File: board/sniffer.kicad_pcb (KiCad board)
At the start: 8 copper layers, 154 x 125 mm, 321 parts, among them J1 BARREL, J10 CONN_SFP_HOST, J11 SFP_CAGE, J12 PMOD_HOST, J13 CONN_SATA_DEVICE, J14 CONN_SATA_HOST, J15 CONN_LVDS_EXPANSION_HOST, J2 32K243-40ML5, J3 BEL_FUSE_0826-1G1T-23-F, J4 XILINX_JTAG, J5 32K243-40ML5, J6 32K243-40ML5, J7 32K243-40ML5, J8 CONN_SFF8087, J9 CONN_SFF8087, M1 SCREW_HOLE, M2 SCREW_HOLE, M3 SCREW_HOLE, M4 SCREW_HOLE, Q1 SSM6N58NU, U1 OKL-T_3-W12P-C, U10 KSZ9031RN, U11 74AVCH1T45, U12 74AVCH1T45, U13 74AVCH1T45, U14 74AVCH1T45, U15 W25Q128JV, U16 FPF2498, U17 FPF2498, U18 LP2996A, U19 SIT9121AI-2BF-XXS200.000000G, U2 LTC3374-QFN, U3 MYTNA1R84RELA2RA, U4 DDR3_SODIMM, U5 XC7K70T-2FBG484, U6 ECX2-LMV-7CN-156.250-TR, U7 SIT9121AI-2BF-XXS200.000000G, U8 ECX2-LMV-3CN-125.000-TR, U9 ECS-2016MVQ-250-CN

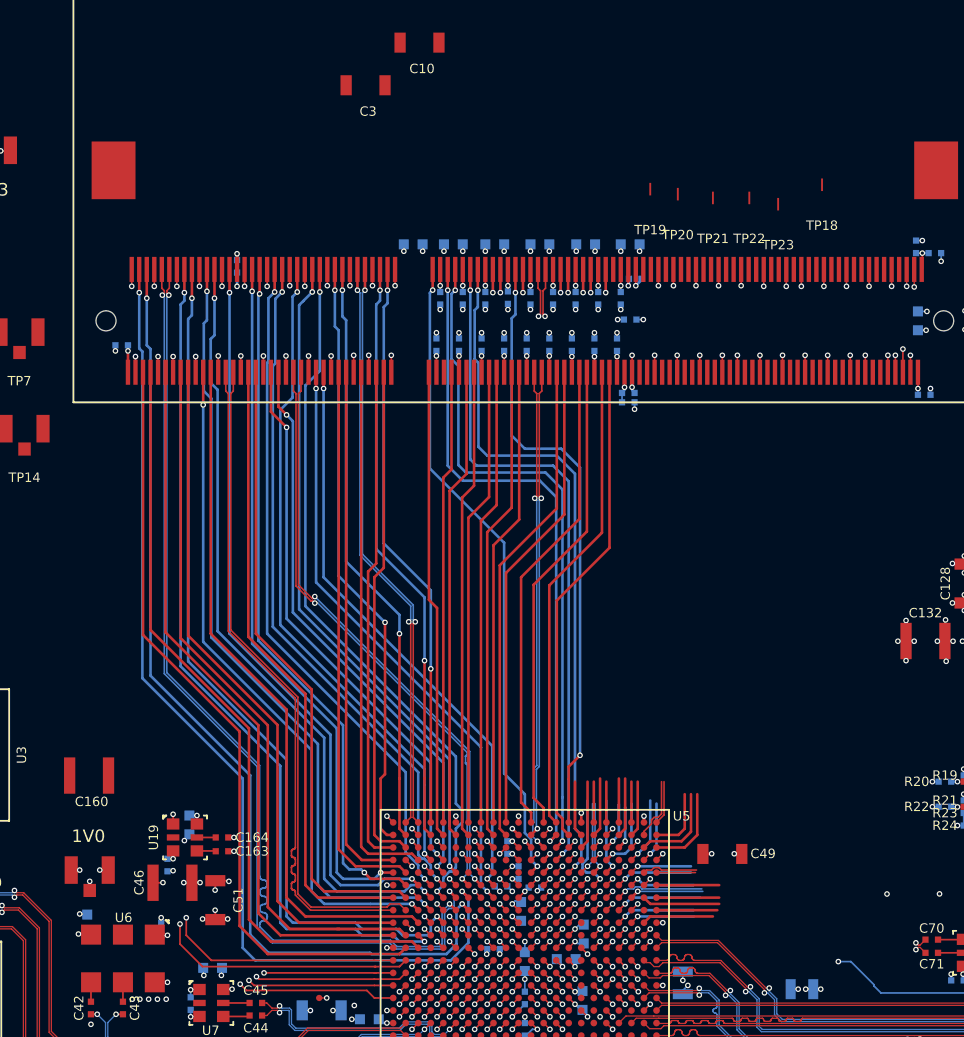
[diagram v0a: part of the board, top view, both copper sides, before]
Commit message: Fully routed DDR. Length matched first three DQ groups.
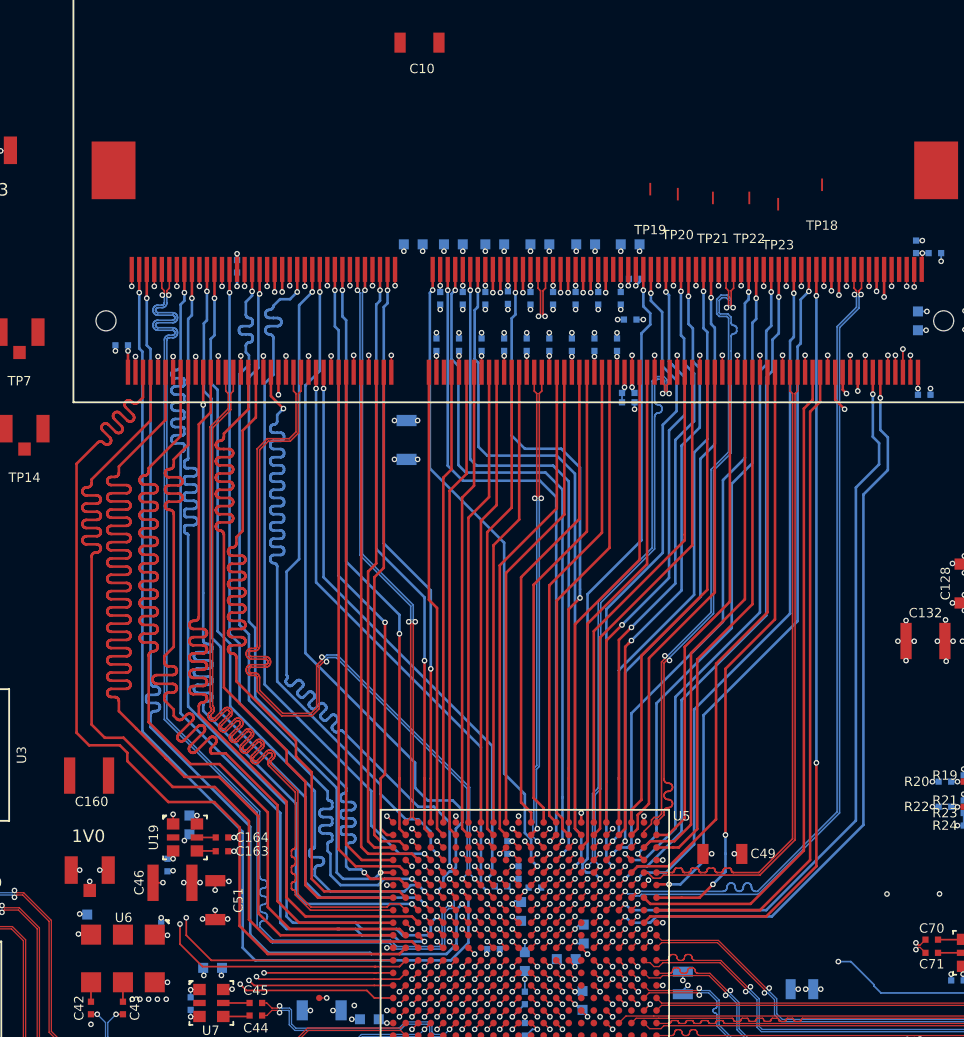
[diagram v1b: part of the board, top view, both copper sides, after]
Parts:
- C3: moved to B.Cu
- moved C3 28.5 mm to (99.5, 75.5), turned to 270 degrees
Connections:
- U5 pad AA16: /DDR/RAM_DQ6_5 -> /DDR/RAM_DQ6_2
- U5 pad AA19: /DDR/RAM_DQ5_3 -> /DDR/RAM_DQ5_7
- U5 pad AA20: /DDR/RAM_DQ5_1 -> /DDR/RAM_DQ5_2
- U5 pad AB16: /DDR/RAM_DQ6_4 -> /DDR/RAM_DQ6_1
- U5 pad AB20: /DDR/RAM_DQ5_4 -> /DDR/RAM_DQ5_3
- U5 pad AB21: /DDR/RAM_DQ5_2 -> /DDR/RAM_DM5
- U5 pad R16: /DDR/RAM_DQ7_0 -> /DDR/RAM_DQ7_4
- U5 pad T15: /DDR/RAM_DQ7_6 -> /DDR/RAM_DQ7_1
- U5 pad T16: /DDR/RAM_DQ7_1 -> /DDR/RAM_DQ7_5
- U5 pad T20: /DDR/RAM_DQ4_7 -> /DDR/RAM_DQ4_1
- U5 pad T21: /DDR/RAM_DM4 -> /DDR/RAM_DQ4_0
- U5 pad U16: /DDR/RAM_DM7 -> /DDR/RAM_DQ7_6
- U5 pad U17: /DDR/RAM_DQ4_5 -> /DDR/RAM_DQ4_4
- U5 pad U21: /DDR/RAM_DQ4_0 -> /DDR/RAM_DQ4_3
- U5 pad U22: /DDR/RAM_DQ4_1 -> /DDR/RAM_DQ4_2
- U5 pad V15: /DDR/RAM_DQ7_4 -> /DDR/RAM_DQ7_0
- U5 pad V18: /DDR/RAM_DQ4_6 -> /DDR/RAM_DQ4_5
- U5 pad V19: /DDR/RAM_DQ5_7 -> /DDR/RAM_DQ5_6
- U5 pad V20: /DDR/RAM_DQ5_5 -> /DDR/RAM_DQ5_4
- U5 pad V22: /DDR/RAM_DQ4_2 -> /DDR/RAM_DM4
- U5 pad W14: /DDR/RAM_DQ7_2 -> /DDR/RAM_DQ7_3
- U5 pad W15: /DDR/RAM_DQ7_5 -> /DDR/RAM_DQ7_2
- U5 pad W17: /DDR/RAM_DQ6_1 -> /DDR/RAM_DQ6_5
- U5 pad W20: /DDR/RAM_DQ5_6 -> /DDR/RAM_DQ5_5
- U5 pad W21: /DDR/RAM_DQ4_3 -> /DDR/RAM_DQ4_7
- U5 pad W22: /DDR/RAM_DQ4_4 -> /DDR/RAM_DQ4_6
- U5 pad Y14: /DDR/RAM_DQ7_3 -> /DDR/RAM_DM7
- U5 pad Y17: /DDR/RAM_DQ6_2 -> /DDR/RAM_DM6
- U5 pad Y18: /DDR/RAM_DM6 -> /DDR/RAM_DQ6_0
- U5 pad Y19: /DDR/RAM_DQ6_0 -> /DDR/RAM_DQ6_4
- U5 pad Y21: /DDR/RAM_DM5 -> /DDR/RAM_DQ5_1
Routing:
- net /Power Supply/1V0_GOOD: track 23.0 -> 118.0 mm
- net /DDR/RAM_DQS7_N: track 5.90 -> 64.9 mm, vias 1 -> 2
- net /DDR/RAM_DQS7_P: track 7.03 -> 64.9 mm, vias 1 -> 2
- net /DDR/RAM_DQ6_7: track 5.71 -> 63.2 mm, vias 0 -> 2
- net /DDR/RAM_DQ7_3: track 5.21 -> 60.3 mm, vias 1 -> 2
- net /DDR/RAM_DQ7_7: track 6.27 -> 61.0 mm, vias 1 -> 2
- net /DDR/RAM_DQ7_4: track 4.41 -> 58.8 mm, vias 1 -> 2
- net /DDR/RAM_DQ7_6: track 6.62 -> 59.4 mm, vias 1 -> 2
- net /DDR/RAM_DQ7_2: track 6.41 -> 59.0 mm, vias 1 -> 2
- net /DDR/RAM_DQ7_5: track 6.91 -> 58.6 mm, vias 1 -> 2
- net /DDR/RAM_DM6: track 4.96 -> 55.5 mm, vias 1 -> 2
- net /DDR/RAM_DQ6_6: track 5.00 -> 55.2 mm, vias 0 -> 2
- net /DDR/RAM_DQ4_4: track 3.50 -> 52.7 mm, vias 0 -> 2
- net /DDR/RAM_DQ5_6: track 3.46 -> 52.2 mm, vias 1 -> 2
- net /DDR/RAM_DQ6_4: track 5.00 -> 53.7 mm, vias 0 -> 2
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
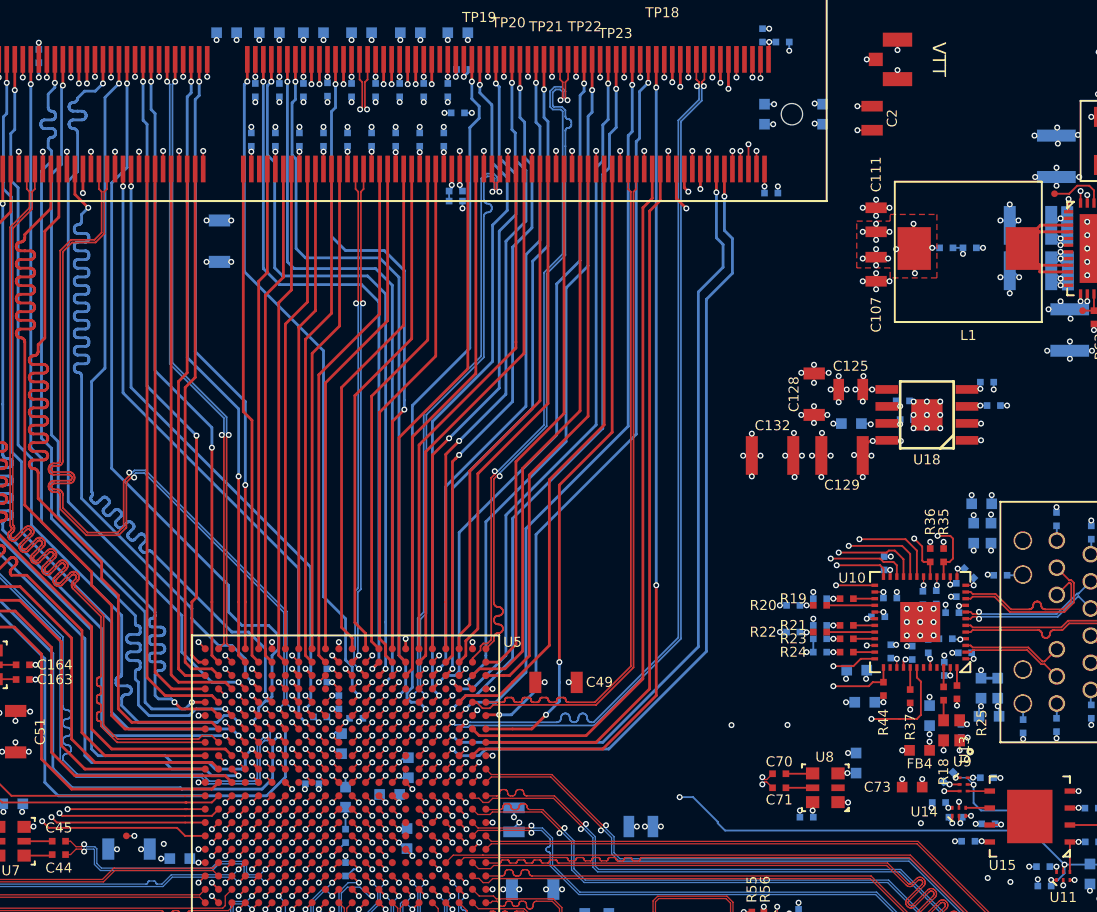
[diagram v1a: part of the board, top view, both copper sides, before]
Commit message: Continued work on layout. Finished length matchnig all DQ byte groups. Still have to do C/A bus.
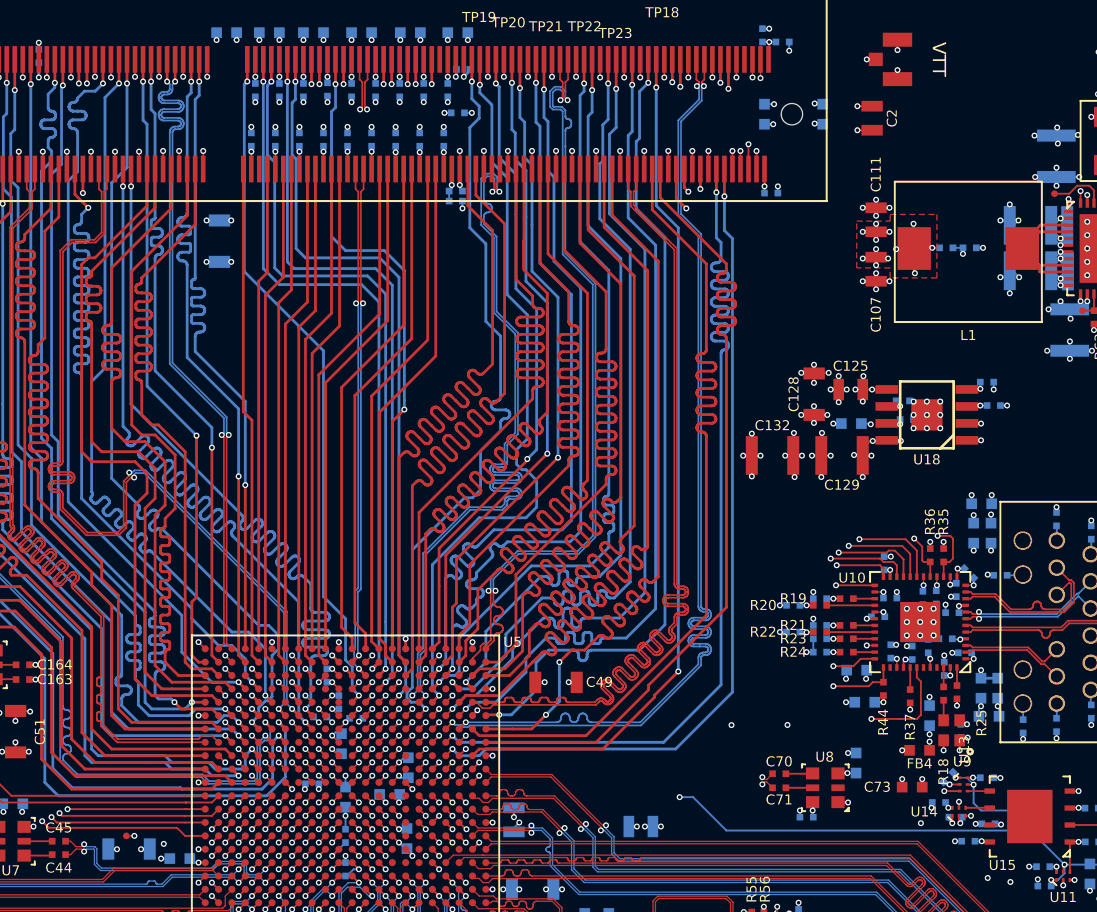
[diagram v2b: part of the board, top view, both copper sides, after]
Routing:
- net /DDR/RAM_DQ4_3: track 40.2 -> 63.6 mm
- net /DDR/RAM_DQ6_0: track 45.9 -> 67.0 mm
- net /DDR/RAM_DQ5_1: track 39.7 -> 59.7 mm
- net /DDR/RAM_DQ5_0: track 38.4 -> 58.0 mm
- net /DDR/RAM_DQ5_2: track 42.4 -> 61.9 mm
- net /DDR/RAM_DQ2_3: track 46.8 -> 66.4 mm
- net /DDR/RAM_DM5: track 39.9 -> 59.1 mm
- net /DDR/RAM_DQS6_P: track 50.9 -> 70.0 mm
- net /DDR/RAM_DQS6_N: track 50.8 -> 70.0 mm
- net /DDR/RAM_DQ4_1: track 40.1 -> 59.2 mm
- net /DDR/RAM_DQ2_2: track 47.8 -> 66.4 mm
- net /DDR/RAM_DQ5_3: track 42.1 -> 60.4 mm
- net /DDR/RAM_DQ4_0: track 39.2 -> 57.1 mm
- net /DDR/RAM_DQ7_0: track 51.7 -> 67.9 mm
- net /DDR/RAM_DQ4_2: track 38.9 -> 54.7 mm
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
